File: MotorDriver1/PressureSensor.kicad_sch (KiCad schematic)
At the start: 11 parts, among them IC2 mcp6004-e_p, J2 Conn_01x02, J3 Conn_01x02

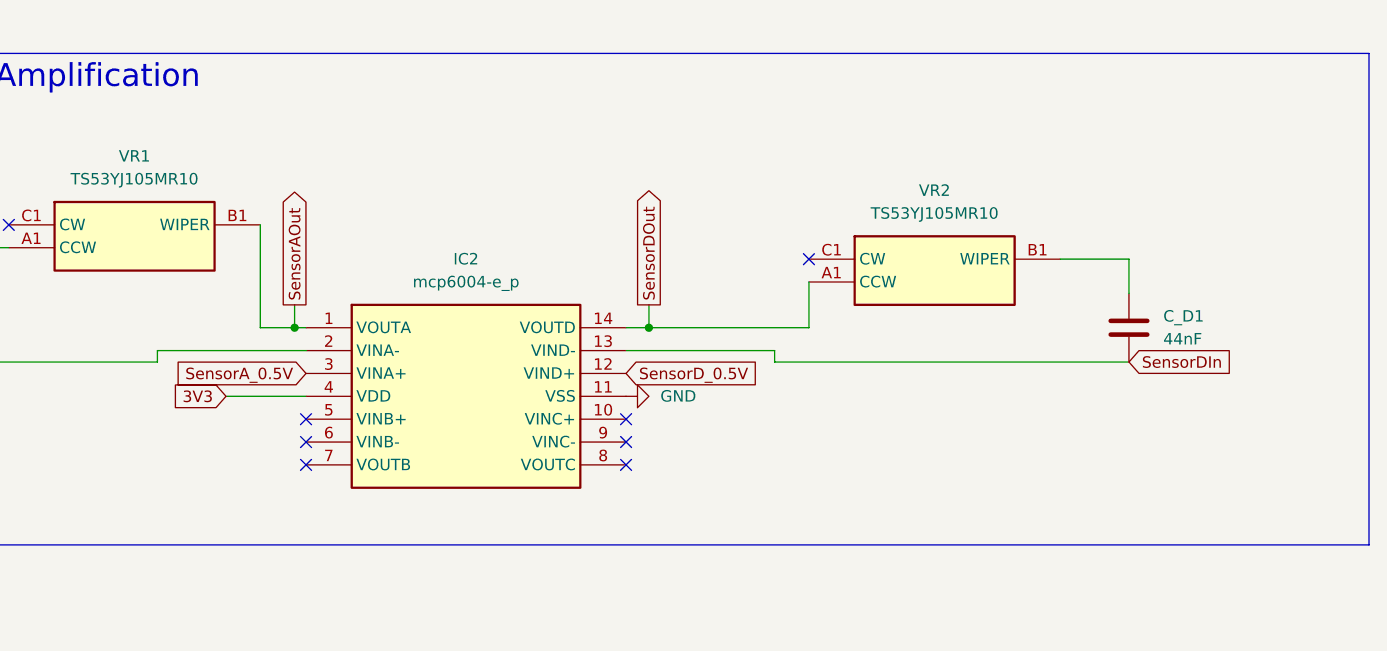
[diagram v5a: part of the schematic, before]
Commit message: component placing and first traces
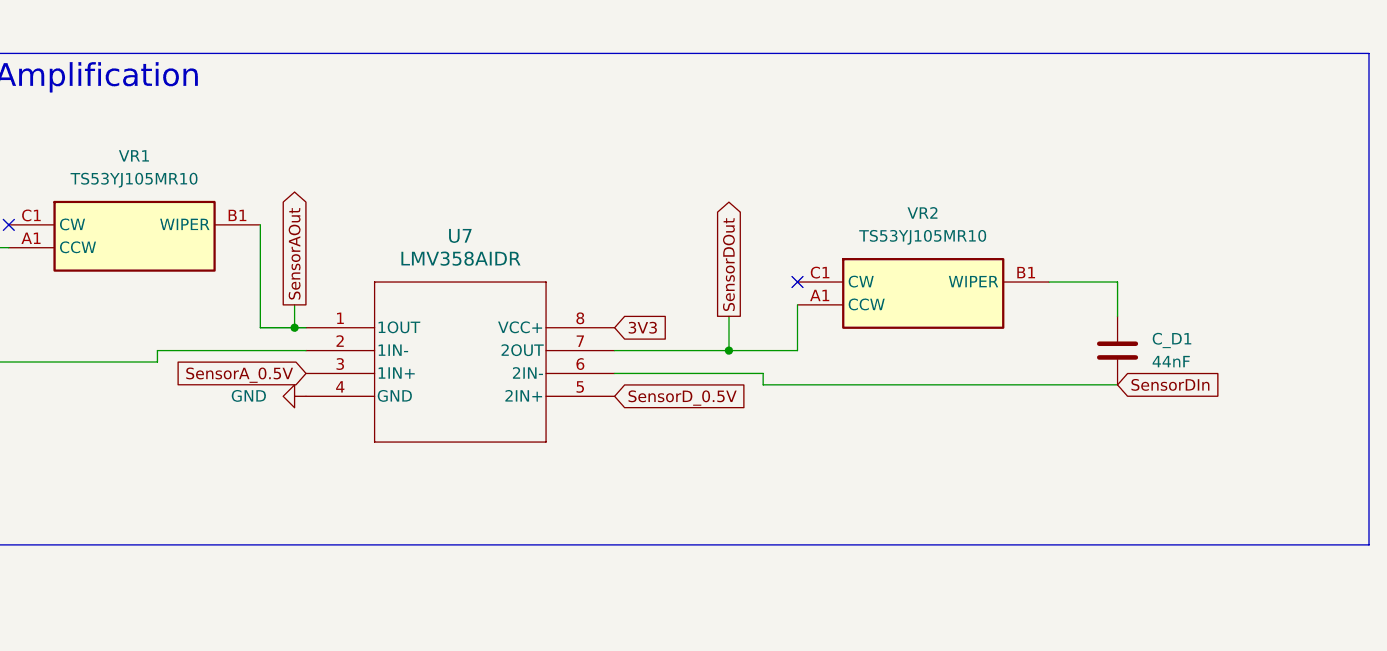
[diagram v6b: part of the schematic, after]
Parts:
- removed IC2: mcp6004-e_p, footprintLib:DIP781W56P254L1918H533Q14N, symbol pcb:mcp6004-e_p
- added U7: LMV358AIDR, footprintLib:D8_TEX, symbol pcb:LMV358AIDR
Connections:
- net 3V3: now also U7.8 (VCC+)
- net GND: now also U7.4 (GND)
- net SensorAIn: now also U7.2 (1IN-)
- net SensorAOut: now also U7.1 (1OUT)
- net SensorA_0.5V: now also U7.3 (1IN+)
- net SensorDIn: now also U7.6 (2IN-)
- net SensorDOut: now also U7.7 (2OUT)
- net SensorD_0.5V: now also U7.5 (2IN+)
- no-connect marks 8 -> 2
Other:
- moved on the sheet: C_D1, VR2

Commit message: Exported final JLCPCB files
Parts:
- added C17: 100 nF, Capacitor_SMD:C_0402_1005Metric, symbol Device:C
- C_A1, C_D1: value 44nF -> 47 nF; footprint Capacitor_SMD:C_0201_0603Metric -> Capacitor_SMD:C_0402_1005Metric
- R16, R17: value 10000 -> 10k
- R18, R19: value 1800 -> 1.8k
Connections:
- net 3V3: now also C17.1
- net GND: now also C17.2
- net SensorAIn: now also C_A1.2, VR1.A1 (CCW); no longer C_A1.1
- net SensorAOut: now also C_A1.1
- net SensorDIn: now also VR2.A1 (CCW)
- net SensorDOut: now also C_D1.2, VR2.B1 (WIPER); no longer VR2.A1 (CCW)
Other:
- moved on the sheet: C_A1, C_D1, VR1, VR2

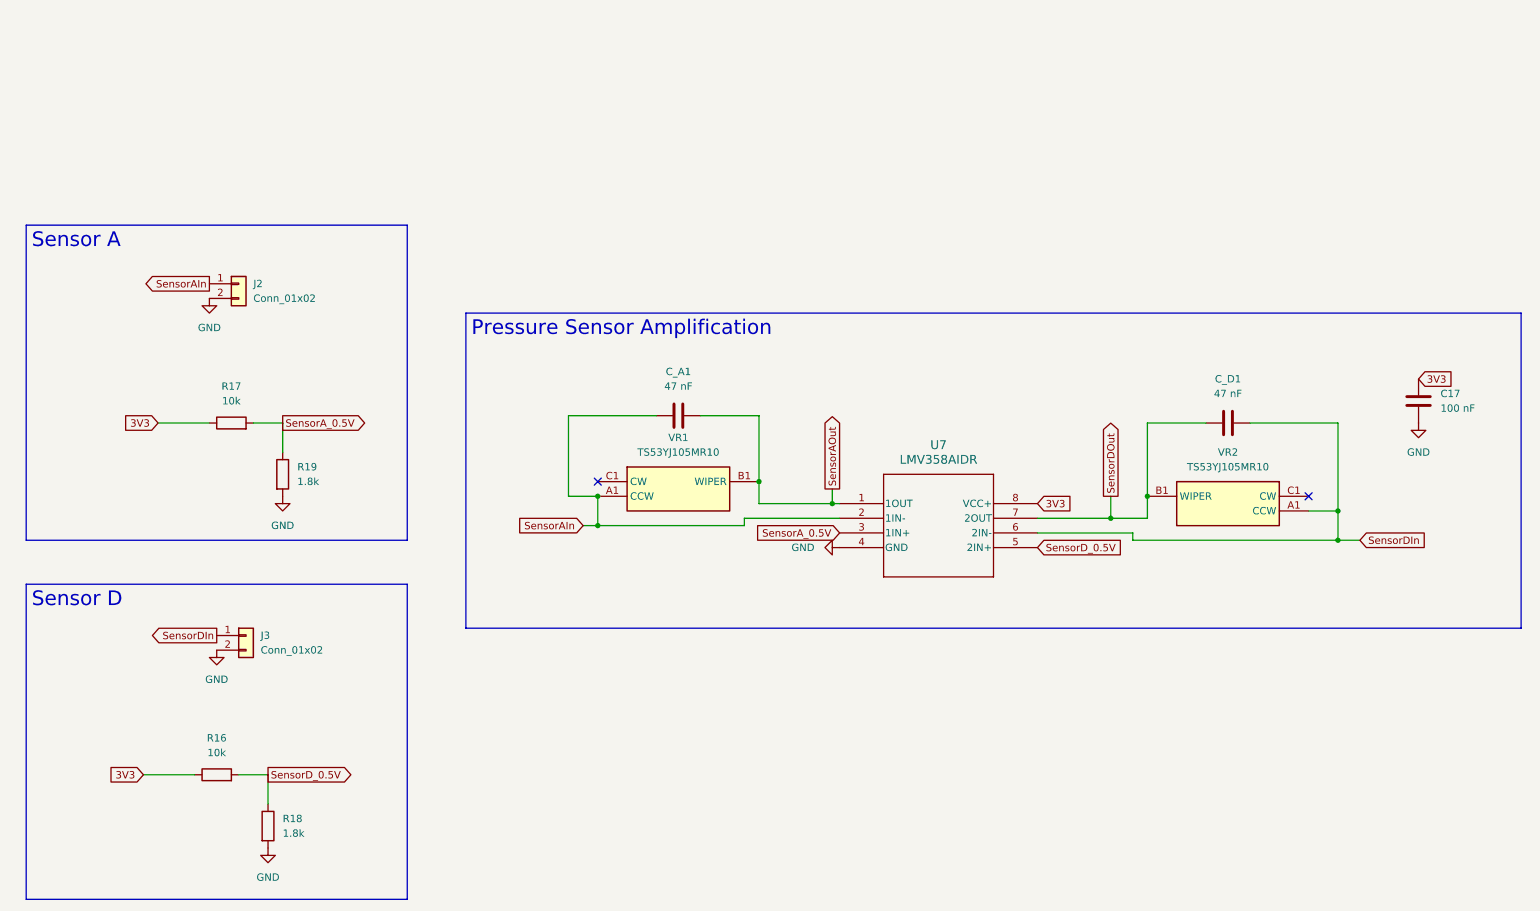
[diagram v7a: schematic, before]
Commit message: added motors and sensors for 4 pad system
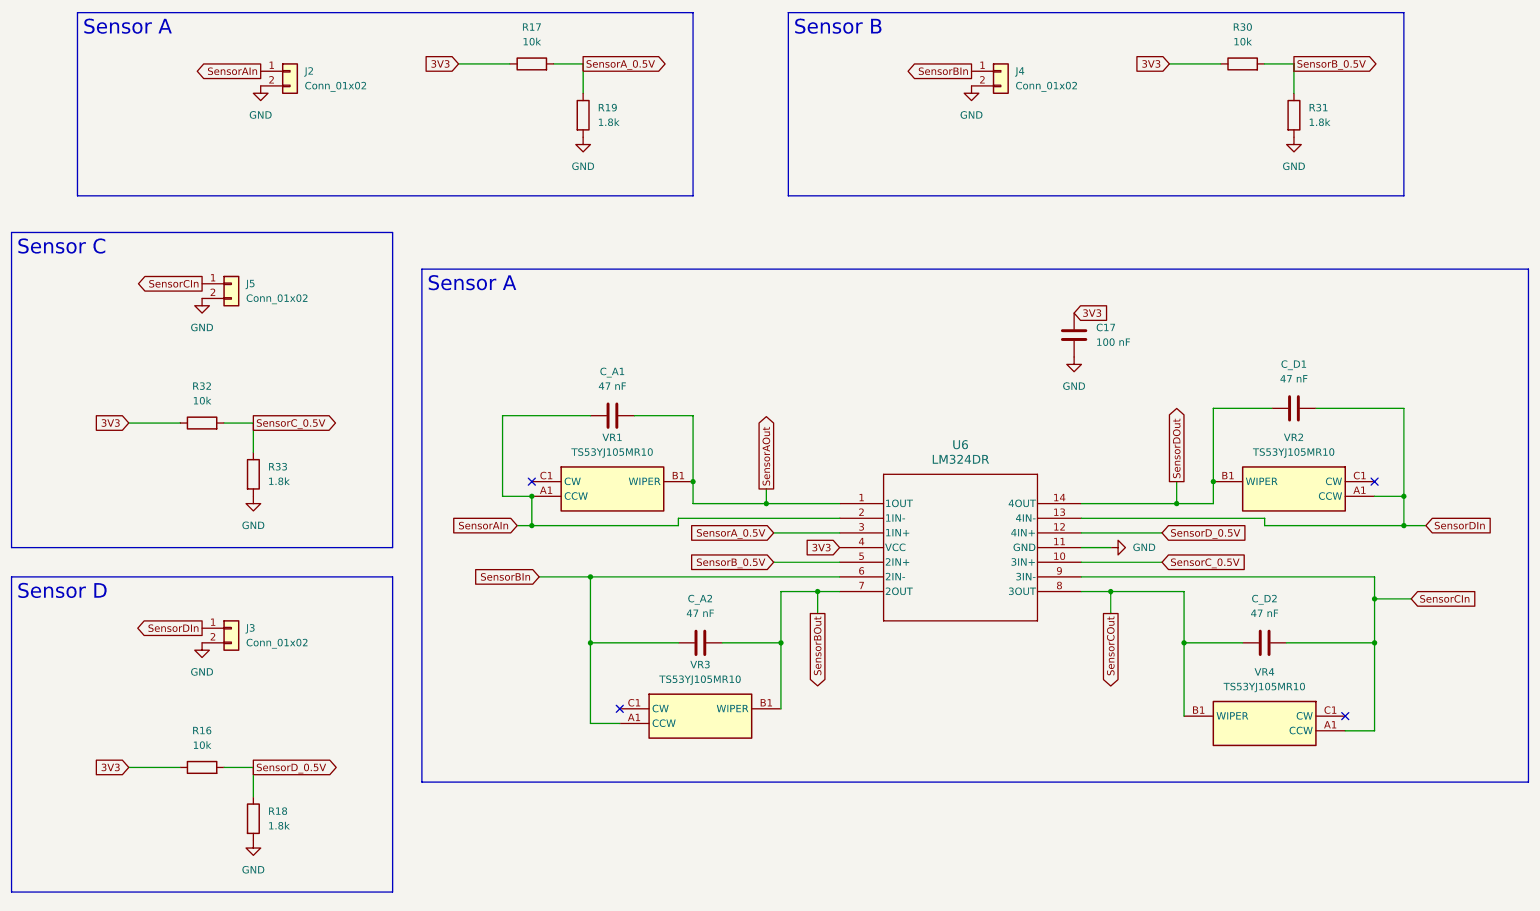
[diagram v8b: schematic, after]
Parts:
- removed U7: LMV358AIDR, footprintLib:D8_TEX, symbol pcb:LMV358AIDR
- added C_A2, C_D2: 47 nF, Capacitor_SMD:C_0402_1005Metric, symbol Device:C
- added J4, J5: Conn_01x02, Connector_PinHeader_2.54mm:PinHeader_1x02_P2.54mm_Vertical, symbol Connector_Generic:Conn_01x02
- added R30, R32: 10k, Resistor_SMD:R_0402_1005Metric, symbol Device:R
- added R31, R33: 1.8k, Resistor_SMD:R_0402_1005Metric, symbol Device:R
- added U6: LM324DR, footprintLib:D14, symbol pcb:LM324DR
- added VR3, VR4: TS53YJ105MR10, footprintLib:TS53YJ105MR10, symbol pcb:TS53YJ105MR10
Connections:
- net 3V3: now also R30.1, R32.1, U6.4 (VCC)
- net GND: now also J4.2 (Pin_2), J5.2 (Pin_2), R31.2, R33.2, U6.11 (GND)
- net SensorAIn: now also U6.2 (1IN-)
- net SensorAOut: now also U6.1 (1OUT)
- net SensorA_0.5V: now also U6.3 (1IN+)
- net SensorDIn: now also U6.13 (4IN-)
- net SensorDOut: now also U6.14 (4OUT)
- net SensorD_0.5V: now also U6.12 (4IN+)
- new net SensorBIn: C_A2.2, J4.1 (Pin_1), U6.6 (2IN-), VR3.A1 (CCW)
- new net SensorBOut: C_A2.1, U6.7 (2OUT), VR3.B1 (WIPER)
- new net SensorB_0.5V: R30.2, R31.1, U6.5 (2IN+)
- new net SensorCIn: C_D2.1, J5.1 (Pin_1), U6.9 (3IN-), VR4.A1 (CCW)
- new net SensorCOut: C_D2.2, U6.8 (3OUT), VR4.B1 (WIPER)
- new net SensorC_0.5V: R32.2, R33.1, U6.10 (3IN+)
- no-connect marks 2 -> 4
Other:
- moved on the sheet: C17, C_A1, C_D1, J2, J3, R16, R17, R18, R19, VR1, VR2
